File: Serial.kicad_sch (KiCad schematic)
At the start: 10 parts

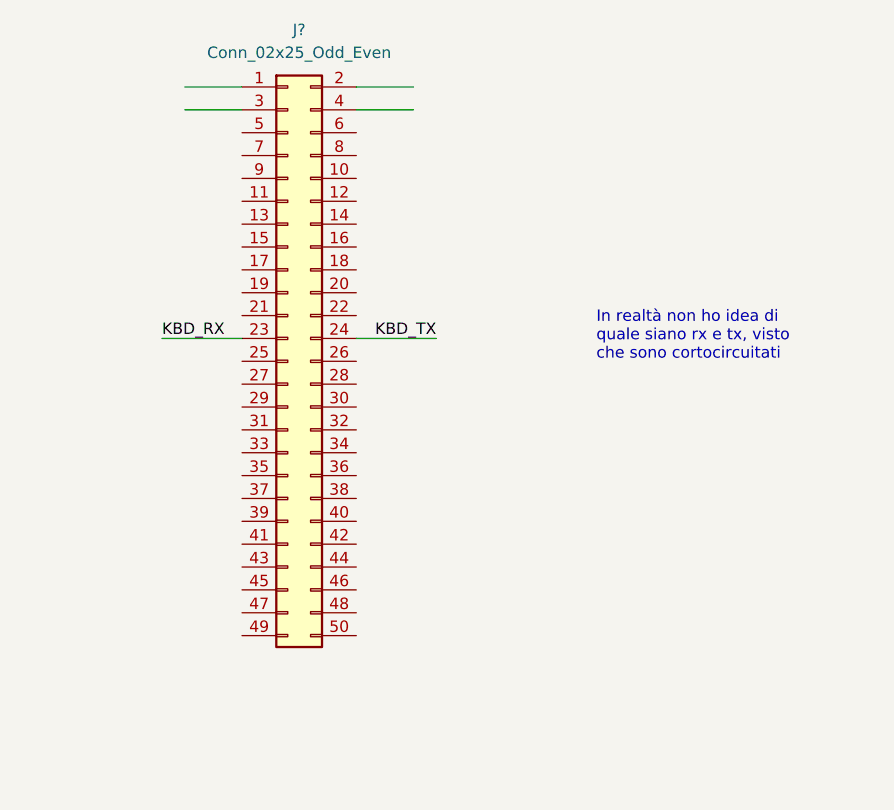
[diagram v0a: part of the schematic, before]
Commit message: Add daughterboard schematics.
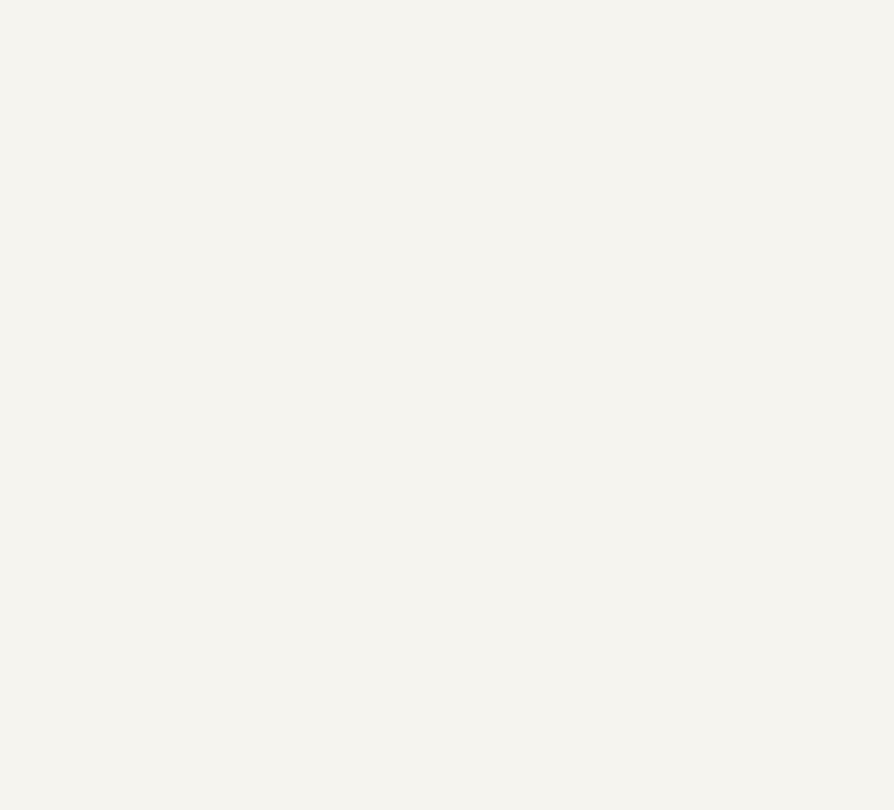
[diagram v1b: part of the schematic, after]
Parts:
- removed J?: Conn_02x25_Odd_Even, symbol Connector_Generic:Conn_02x25_Odd_Even
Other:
- note removed: "In realtà non ho idea di quale siano rx e tx, visto che sono cortocircuitati"
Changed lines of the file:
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@@
-    (stroke (width 0) (type default) (color 0 0 0 0))
-  )
-  (wire (pts (xy 232.41 41.91) (xy 238.76 41.91))
     (stroke (width 0) (type default) (color 0 0 0 0))
   )
@@
     (stroke (width 0) (type default) (color 0 0 0 0))
   )
-  (wire (pts (xy 232.41 44.45) (xy 238.76 44.45))
-    (stroke (width 0) (type default) (color 0 0 0 0))
-  )
-  (wire (pts (xy 251.46 69.85) (xy 260.35 69.85))
-    (stroke (width 0) (type default) (color 0 0 0 0))
-  )
   (wire (pts (xy 101.6 101.6) (xy 101.6 102.87))
     (stroke (width 0) (type default) (color 0 0 0 0))
@@
     (stroke (width 0) (type default) (color 0 0 0 0))
   )
-  (wire (pts (xy 251.46 44.45) (xy 257.81 44.45))
-    (stroke (width 0) (type default) (color 0 0 0 0))
-  )
   (wire (pts (xy 167.64 72.39) (xy 167.64 78.74))
     (stroke (width 0) (type default) (color 0 0 0 0))
@@
     (stroke (width 0) (type default) (color 0 0 0 0))
   )
-  (wire (pts (xy 251.46 41.91) (xy 257.81 41.91))
-    (stroke (width 0) (type default) (color 0 0 0 0))
-  )
   (wire (pts (xy 118.11 81.28) (xy 118.11 78.74))
     (stroke (width 0) (type default) (color 0 0 0 0))
@@
     (stroke (width 0) (type default) (color 0 0 0 0))
   )
-  (wire (pts (xy 229.87 69.85) (xy 238.76 69.85))
-    (stroke (width 0) (type default) (color 0 0 0 0))
-  )
   (text "153.6 kHz" (at 104.14 114.3 0)
     (effects (font (size 1.27 1.27)) (justify left bottom))
@@
     (effects (font (size 1.27 1.27)) (justify left bottom))
   )
-  (text "In realtà non ho idea di\nquale siano rx e tx, visto\nche sono cortocircuitati"
-    (at 278.13 72.39 0)
-    (effects (font (size 1.27 1.27)) (justify left bottom))
-  )
   (text "153.6 kHz" (at 71.12 134.62 0)
     (effects (font (size 1.27 1.27)) (justify left bottom))
@@
     (effects (font (size 1.27 1.27)) (justify left bottom))
   )
-  (label "KBD_RX" (at 229.87 69.85 0)
-    (effects (font (size 1.27 1.27)) (justify left bottom))
-  )
   (label "KBD_TX" (at 194.31 78.74 180)
     (effects (font (size 1.27 1.27)) (justify right bottom))
@@
   (label "addr0" (at 30.48 167.64 0)
     (effects (font (size 1.27 1.27)) (justify left bottom))
-  )
-  (label "KBD_TX" (at 260.35 69.85 180)
-    (effects (font (size 1.27 1.27)) (justify right bottom))
   )
   (global_label "SystemBus" (shape bidirectional) (at 26.67 119.38 180) (fields_autoplaced)
@@
     (pin "1")
   )
-  (symbol (lib_id "Connector_Generic:Conn_02x25_Odd_Even") (at 243.84 72.39 0) (unit 1)
-    (in_bom yes) (on_board yes) (fields_autoplaced)
-    (property "Reference" "J?" (id 0) (at 245.11 35.56 0))
-    (property "Value" "Conn_02x25_Odd_Even" (id 1) (at 245.11 38.1 0))
-    (property "Footprint" "" (id 2) (at 243.84 72.39 0)
-      (effects (font (size 1.27 1.27)) hide)
-    )
-    (property "Datasheet" "~" (id 3) (at 243.84 72.39 0)
-      (effects (font (size 1.27 1.27)) hide)
-    )
-    (pin "1")
-    (pin "10")
-    (pin "11")
-    (pin "12")
-    (pin "13")
-    (pin "14")
-    (pin "15")
-    (pin "16")
-    (pin "17")
-    (pin "18")
-    (pin "19")
-    (pin "2")
-    (pin "20")
-    (pin "21")
-    (pin "22")
-    (pin "23")
-    (pin "24")
-    (pin "25")
-    (pin "26")
-    (pin "27")
-    (pin "28")
-    (pin "29")
-    (pin "3")
-    (pin "30")
-    (pin "31")
-    (pin "32")
-    (pin "33")
-    (pin "34")
-    (pin "35")
-    (pin "36")
-    (pin "37")
-    (pin "38")
-    (pin "39")
-    (pin "4")
-    (pin "40")
-    (pin "41")
-    (pin "42")
-    (pin "43")
-    (pin "44")
-    (pin "45")
-    (pin "46")
-    (pin "47")
-    (pin "48")
-    (pin "49")
-    (pin "5")
-    (pin "50")
-    (pin "6")
-    (pin "7")
-    (pin "8")
-    (pin "9")
-  )
   (symbol (lib_id "Jumper:Jumper_2_Bridged") (at 167.64 67.31 270) (mirror x) (unit 1)

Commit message: Reset circuit
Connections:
- net ~{RESET}: now reaches U?.21 (~{RESET})
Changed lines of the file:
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@@
+    (stroke (width 0) (type default))
+  )
+  (wire (pts (xy 30.48 154.94) (xy 38.1 154.94))
     (stroke (width 0) (type default))
   )
@@
     (effects (font (size 1.27 1.27)) (justify left bottom))
   )
+  (label "~{RESET}" (at 30.48 154.94 0) (fields_autoplaced)
+    (effects (font (size 1.27 1.27)) (justify left bottom))
+  )

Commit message: IO addressing space multiplexing and small IO description
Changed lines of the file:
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@@
+    (stroke (width 0) (type default))
+  )
+  (wire (pts (xy 30.48 152.4) (xy 38.1 152.4))
     (stroke (width 0) (type default))
   )
@@
   (symbol (lib_id "ceda:Z8440{slash}2") (at 53.34 152.4 0) (unit 1)
     (in_bom yes) (on_board yes) (dnp no) (fields_autoplaced)
-    (property "Reference" "U?" (at 53.34 177.8 0)
-      (effects (font (size 1.27 1.27)))
-    )
-    (property "Value" "Z8440/2 (SIO/2)" (at 53.34 151.13 90)
-      (effects (font (size 1.27 1.27)))
+    (property "Reference" "U?" (at 55.5341 118.11 0)
+      (effects (font (size 1.27 1.27)) (justify left))
+    )
+    (property "Value" "Z8440/2 (SIO/2)" (at 55.5341 120.65 0)
+      (effects (font (size 1.27 1.27)) (justify left))
     )
     (property "Footprint" "" (at 47.625 137.795 0)

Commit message: Serial communication interface
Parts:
- removed JP? (x2): Jumper_2_Bridged, symbol Jumper:Jumper_2_Bridged
- added A15, C15: ~, symbol ceda:SN74189
- added C10, C3, C4, C5, C6, C8, C9: xxxn, symbol Device:C
- added unit 2 of D14
- added D15, D16: ~, symbol ceda:SN75188
- added UB9: 74LS04, symbol 74xx:74LS04
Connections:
- net VCC: no longer U?.9 (VCC)
- net RxCA: now reaches J?.1 (A0)
- net RxCA: now also U?.13 (~{RxCA})
- net TxCA: now reaches J?.2 (B0)
- net TxCA: now also J?.3 (C0), U?.14 (~{TxCA})
- net TxCA'': now reaches J?.4 (C1)
- net TxCA'': now also D15.12, D15.13
- net TxCA': now reaches J?.5 (B1)
- net TxCA': now also A15.8
- net RxCA': now reaches J?.6 (A1)
- net RxCA': now also A15.11
- net RxDA: now reaches U?.12 (RxDA)
- net RxDA: now also C15.3
- net TxDA: now reaches U?.15 (TxDA)
- net TxDA: now also D15.2
- net ~{DTRA}: now reaches U?.16 (~{DTRA})
- net ~{DTRA}: now also D15.10, D15.9
- net ~{RTSA}: now reaches U?.17 (~{RTSA})
- net ~{RTSA}: now also D15.4, D15.5
- net ~{CTSA}: now reaches U?.18 (~{CTSA})
- net ~{CTSA}: now also C15.6
- net ~{DCDA}: now reaches U?.19 (~{DCDA})
- net ~{DCDA}: now also C15.8
- net ~{DCDB}: now reaches U?.22 (~{DCDB})
- net ~{DCDB}: now also A15.3
- net ~{CTSB}: now reaches U?.23 (~{CTSB})
- net ~{CTSB}: now also A15.6
- net ~{DTRB}: now reaches U?.25 (~{DTRB})
- net ~{DTRB}: now also D14.2, UB9.1
- net RxDB: now reaches U?.29 (RxDB)
- net RxDB: now also D14.11
- net ~{SIO_CS}: now reaches U?.35 (~{CE})
- net ~{IORQ}: now reaches U?.36 (~{IORQ})
- net SIO_26_TXDB renamed TxDB
- net TxDB: now also D14.4
- net SIO_27_~{TXCB} renamed ~{TxCB}
- net ~{TxCB}: now also U?.28 (~{RxCB}); no longer D14.2
- removed net SIO_29_RXDB: D14.11, U?.28 (RxDB)
- new net: C10.2, C15.9
- new net: A15.12, C6.2
- new net: A15.9, C5.2
- new net: D14.6, D16.2
- new net: A15.2, C3.2
- new net: C15.5, C9.2
- new net: D14.5, UB9.2
- new net: A15.5, C4.2
- new net: C15.2, C8.2
- no-connect marks 2 -> 7
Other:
- note added: "188"
- note added: "189"
- note added: "DA VERIFIXARE"
- note removed: "19.2 kHz"

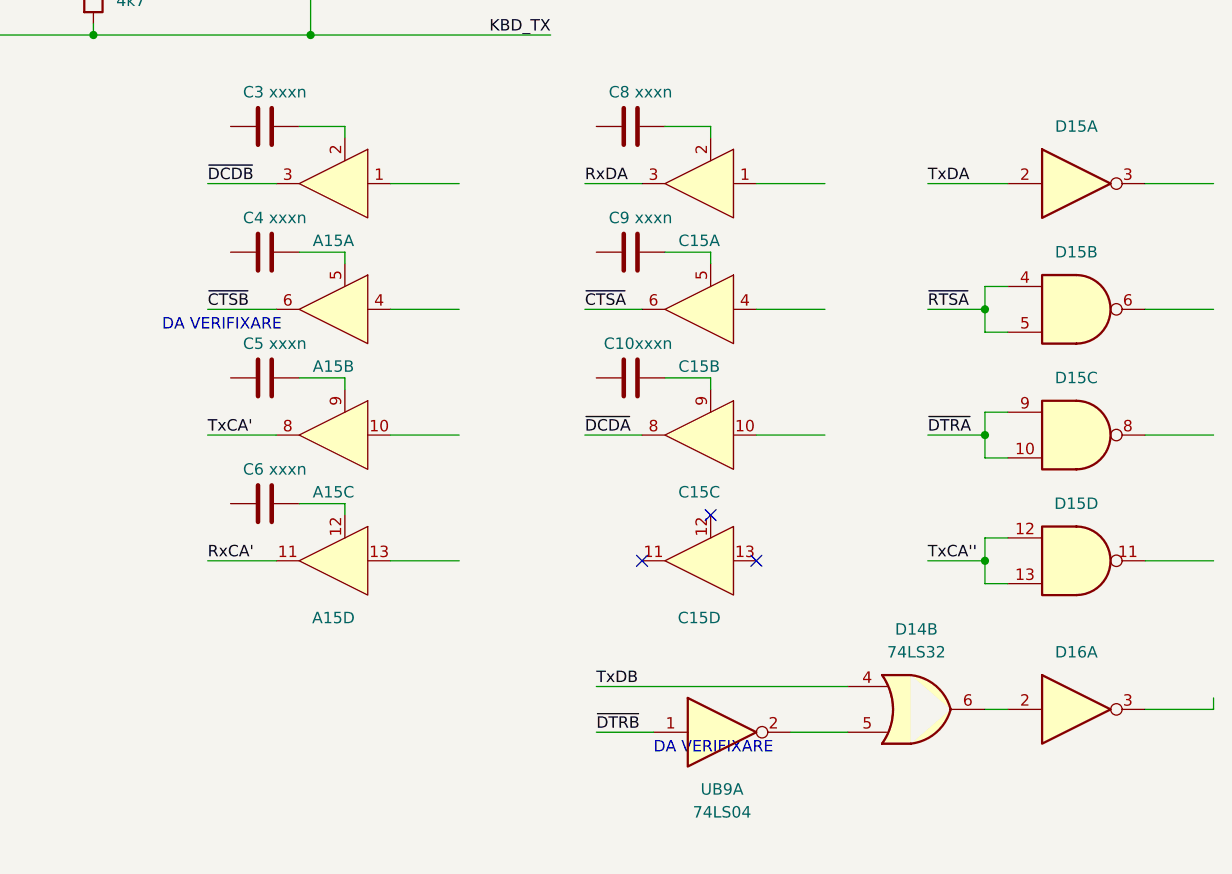
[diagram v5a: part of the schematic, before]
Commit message: parallel port, which is absolutely not a centronics port
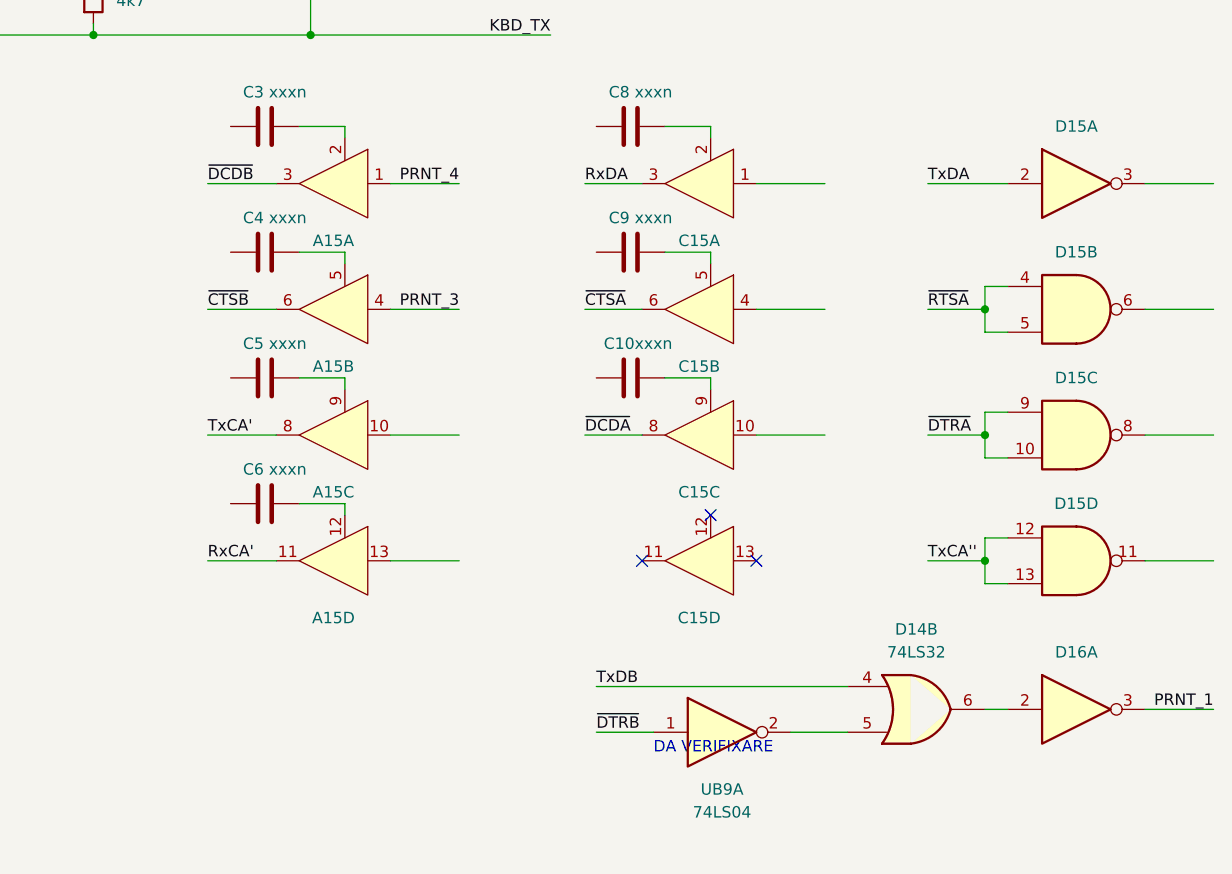
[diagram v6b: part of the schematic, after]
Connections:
- net PRNT_1: now reaches D16.3
- net PRNT_3: now reaches A15.4
- net PRNT_4: now reaches A15.1
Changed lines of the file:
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@@
-    (stroke (width 0) (type default))
-  )
-  (wire (pts (xy 267.97 152.4) (xy 267.97 153.67))
     (stroke (width 0) (type default))
   )
@@
     (effects (font (size 1.27 1.27)) (justify left bottom))
   )
-  (text "DA VERIFIXARE" (at 151.13 111.76 0)
-    (effects (font (size 1.27 1.27)) (justify left bottom))
-  )
   (text "153.6 kHz" (at 88.9 100.33 0)
     (effects (font (size 1.27 1.27)) (justify left bottom))
@@
     (effects (font (size 1.27 1.27)) (justify right bottom))
   )
+  (label "PRNT_4" (at 184.15 95.25 180) (fields_autoplaced)
+    (effects (font (size 1.27 1.27)) (justify right bottom))
+  )
   (label "RxCA'" (at 78.74 119.38 90) (fields_autoplaced)
     (effects (font (size 1.27 1.27)) (justify left bottom))
@@
     (effects (font (size 1.27 1.27)) (justify left bottom))
   )
+  (label "PRNT_3" (at 184.15 109.22 180) (fields_autoplaced)
+    (effects (font (size 1.27 1.27)) (justify right bottom))
+  )
   (label "~{DCDA}" (at 198.12 123.19 0) (fields_autoplaced)
     (effects (font (size 1.27 1.27)) (justify left bottom))
@@
     (effects (font (size 1.27 1.27)) (justify left bottom))
   )
+  (label "PRNT_1" (at 267.97 153.67 180) (fields_autoplaced)
+    (effects (font (size 1.27 1.27)) (justify right bottom))
+  )
   (label "~{DCDA}" (at 82.55 152.4 180) (fields_autoplaced)

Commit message: Removed some dangling notes
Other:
- note removed: "188"
- note removed: "189"
- note removed: "DA VERIFIXARE"
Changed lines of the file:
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@@
     (stroke (width 0) (type default))
   )
-  (wire (pts (xy 69.85 134.62) (xy 93.98 134.62))
+  (wire (pts (xy 69.85 134.62) (xy 82.55 134.62))
     (stroke (width 0) (type default))
   )
@@
     (stroke (width 0) (type default))
   )
-  (wire (pts (xy 69.85 129.54) (xy 93.98 129.54))
+  (wire (pts (xy 69.85 129.54) (xy 82.55 129.54))
     (stroke (width 0) (type default))
   )
@@
     (stroke (width 0) (type default))
   )
-  (wire (pts (xy 69.85 144.78) (xy 93.98 144.78))
+  (wire (pts (xy 69.85 144.78) (xy 82.55 144.78))
     (stroke (width 0) (type default))
   )
@@
     (stroke (width 0) (type default))
   )
-  (wire (pts (xy 69.85 149.86) (xy 105.41 149.86))
+  (wire (pts (xy 69.85 149.86) (xy 82.55 149.86))
     (stroke (width 0) (type default))
   )
@@
     (stroke (width 0) (type default))
   )
-  (wire (pts (xy 69.85 132.08) (xy 105.41 132.08))
+  (wire (pts (xy 69.85 132.08) (xy 82.55 132.08))
     (stroke (width 0) (type default))
   )
@@
     (stroke (width 0) (type default))
   )
-  (text "189" (at 78.74 154.94 0)
-    (effects (font (size 1.27 1.27)) (justify left bottom))
-  )
   (text "153.6 kHz" (at 88.9 100.33 0)
     (effects (font (size 1.27 1.27)) (justify left bottom))
   )
-  (text "188" (at 101.6 154.94 0)
-    (effects (font (size 1.27 1.27)) (justify left bottom))
-  )
   (text "Open Collector" (at 114.3 60.96 0)
     (effects (font (size 1.27 1.27)) (justify left bottom))
   )
-  (text "153.6 kHz" (at 71.12 134.62 0)
-    (effects (font (size 1.27 1.27)) (justify left bottom))
-  )
-  (text "DA VERIFIXARE" (at 205.74 158.75 0)
+  (text "153.6 kHz" (at 83.82 134.62 0)
     (effects (font (size 1.27 1.27)) (justify left bottom))
   )
@@
     (effects (font (size 1.27 1.27)) (justify left bottom))
   )
-  (label "~{DTRA}" (at 105.41 149.86 180) (fields_autoplaced)
+  (label "~{DTRA}" (at 82.55 149.86 180) (fields_autoplaced)
     (effects (font (size 1.27 1.27)) (justify right bottom))
   )
@@
     (effects (font (size 1.27 1.27)) (justify right bottom))
   )
-  (label "~{RTSA}" (at 93.98 144.78 180) (fields_autoplaced)
+  (label "~{RTSA}" (at 82.55 144.78 180) (fields_autoplaced)
     (effects (font (size 1.27 1.27)) (justify right bottom))
   )
@@
     (effects (font (size 1.27 1.27)) (justify right bottom))
   )
-  (label "TxDA" (at 105.41 132.08 180) (fields_autoplaced)
+  (label "TxDA" (at 82.55 132.08 180) (fields_autoplaced)
     (effects (font (size 1.27 1.27)) (justify right bottom))
   )
@@
     (effects (font (size 1.27 1.27)) (justify left bottom))
   )
-  (label "TxCA" (at 93.98 134.62 180) (fields_autoplaced)
+  (label "TxCA" (at 82.55 134.62 180) (fields_autoplaced)
     (effects (font (size 1.27 1.27)) (justify right bottom))
   )
@@
     (effects (font (size 1.27 1.27)) (justify left bottom))
   )
-  (label "RxCA" (at 93.98 129.54 180) (fields_autoplaced)
-    (effects (font (size 1.27 1.27)) (justify right bottom))
-  )
+  (label "RxCA" (at 82.55 129.54 180) (fields_autoplaced)
+    (effects (font (size 1.27 1.27)) (justify right bottom))
+  )
